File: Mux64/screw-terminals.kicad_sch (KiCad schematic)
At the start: 111 parts

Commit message: Add files via upload
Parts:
- gave numbers to parts that had none: 111

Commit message: Add files via upload
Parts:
- J11, J12, J13, J14, J15, J16, J17, J18: footprint (none) -> TerminalBlock_Phoenix:TerminalBlock_Phoenix_MPT-0,5-12-2.54_1x12_P2.54mm_Horizontal
- R10, R100, R101, R102, R103, R104, R105, R106, R107, R108, R109, R11, R110, R12, R13, R14, R15, R16, R17, R18, R19, R20, R21, R22, R23, R24, R25, R26, R27, R28, R29, R30, R31, R32, R39, R40, R41, R42, R43, R44, R45, R46, R47, R48, R49, R50, R57, R58, R59, R60, R61, R62, R63, R64, R65, R66, R67, R68, R69, R70, R71, R72, R73, R74, R75, R76, R77, R78, R79, R80, R81, R82, R83, R84, R85, R86, R87, R88, R89, R9, R90, R91, R92, R93, R94, R95, R96, R97, R98, R99: footprint (none) -> Resistor_SMD:R_0805_2012Metric
- R33, R34, R35, R36, R37, R38, R51, R52, R53, R54, R55, R56: footprint (none) -> Resistor_SMD:R_1206_3216Metric
- R8: footprint (none) -> Resistor_SMD:R_0603_1608Metric

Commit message: Add files via upload
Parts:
- removed R8: 0ohm, Resistor_SMD:R_0603_1608Metric, symbol Device:R_Small_US
- R21, R22, R23, R24, R25, R26: footprint Resistor_SMD:R_0805_2012Metric -> Resistor_SMD:R_1206_3216Metric
- R51, R52, R53, R54, R55, R56: footprint Resistor_SMD:R_1206_3216Metric -> Resistor_SMD:R_0805_2012Metric
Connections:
- net MUX64_A14 is gone; now on net MUX64_A18: R66.2, R77.1
- net MUX64_A28 is gone; now on net MUX64_A29: R49.2, R61.1
- net MUX64_A34 is gone; now on net MUX64_A22: R44.2, R55.1
- net MUX64_A36 is gone; now on net MUX64_A41: R15.2, R27.1
- net MUX64_A10: now also R72.2, R84.1; no longer R109.1, R97.2
- net MUX64_A11: now also R71.2, R83.1; no longer R110.1, R98.2
- net MUX64_A12: now also R70.2, R82.1; no longer R63.2, R75.1
- net MUX64_A13: now also R64.2, R81.1; no longer R65.2, R76.1
- net MUX64_A15: now also R65.2, R76.1; no longer R67.2, R78.1
- net MUX64_A16: now also R63.2, R75.1; no longer R68.2, R79.1
- net MUX64_A17: now also R67.2, R78.1; no longer R69.2, R80.1
- net MUX64_A18: no longer R64.2, R81.1
- net MUX64_A19: now also R69.2, R80.1; no longer R70.2, R82.1
- net MUX64_A2: now also R110.1, R98.2; no longer R101.1, R90.2
- net MUX64_A20: now also R68.2, R79.1; no longer R71.2, R83.1
- net MUX64_A21: now also R45.2, R56.1; no longer R72.2, R84.1
- net MUX64_A22: no longer R73.2, R85.1
- net MUX64_A23: now also R43.2, R54.1; no longer R74.2, R86.1
- net MUX64_A24: now also R42.2, R53.1; no longer R40.2, R57.1
- net MUX64_A25: now also R41.2, R52.1; no longer R46.2, R58.1
- net MUX64_A26: now also R39.2, R51.1; no longer R47.2, R59.1
- net MUX64_A27: now also R50.2, R62.1; no longer R48.2, R60.1
- net MUX64_A29: no longer R50.2, R62.1
- net MUX64_A3: now also R109.1, R97.2; no longer R102.1, R91.2
- net MUX64_A30: now also R48.2, R60.1; no longer R39.2, R51.1
- net MUX64_A31: now also R47.2, R59.1; no longer R41.2, R52.1
- net MUX64_A32: now also R46.2, R58.1; no longer R42.2, R53.1
- net MUX64_A33: now also R40.2, R57.1; no longer R43.2, R54.1
- net MUX64_A35: now also R20.2, R32.1; no longer R45.2, R56.1
- net MUX64_A37: now also R19.2, R31.1; no longer R16.2, R28.1
- net MUX64_A38: now also R18.2, R30.1; no longer R17.2, R29.1
- net MUX64_A39: now also R17.2, R29.1; no longer R18.2, R30.1
- net MUX64_A4: now also R108.1, R96.2; no longer R103.1, R92.2
- net MUX64_A40: now also R16.2, R28.1; no longer R19.2, R31.1
- net MUX64_A41: no longer R20.2, R32.1
- net MUX64_A43: now also R14.2, R26.1; no longer R21.1, R9.2
- net MUX64_A45: now also R13.2, R25.1; no longer R10.2, R22.1
- net MUX64_A47: now also R12.2, R24.1; no longer R11.2, R23.1
- net MUX64_A49: now also R11.2, R23.1; no longer R12.2, R24.1
- net MUX64_A5: now also R107.1, R95.2; no longer R104.1, R93.2
- net MUX64_A51: now also R10.2, R22.1; no longer R13.2, R25.1
- net MUX64_A53: now also R21.1, R9.2; no longer R14.2, R26.1
- net MUX64_A6: now also R106.1, R94.2; no longer R105.1, R88.2
- net MUX64_A7: now also R105.1, R88.2; no longer R106.1, R94.2
- net MUX64_A8: now also R74.2, R86.1; no longer R107.1, R95.2
- net MUX64_A9: now also R73.2, R85.1; no longer R108.1, R96.2
- net MUX64_A0 renamed MUX64_A60
- net MUX64_A1 renamed MUX64_A57
- new net MUX64_A54: R104.1, R93.2
- new net MUX64_A55: R102.1, R91.2
- new net MUX64_A56: R103.1, R92.2
- new net MUX64_A58: R101.1, R90.2
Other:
- note removed: "Unused Mux inputs"

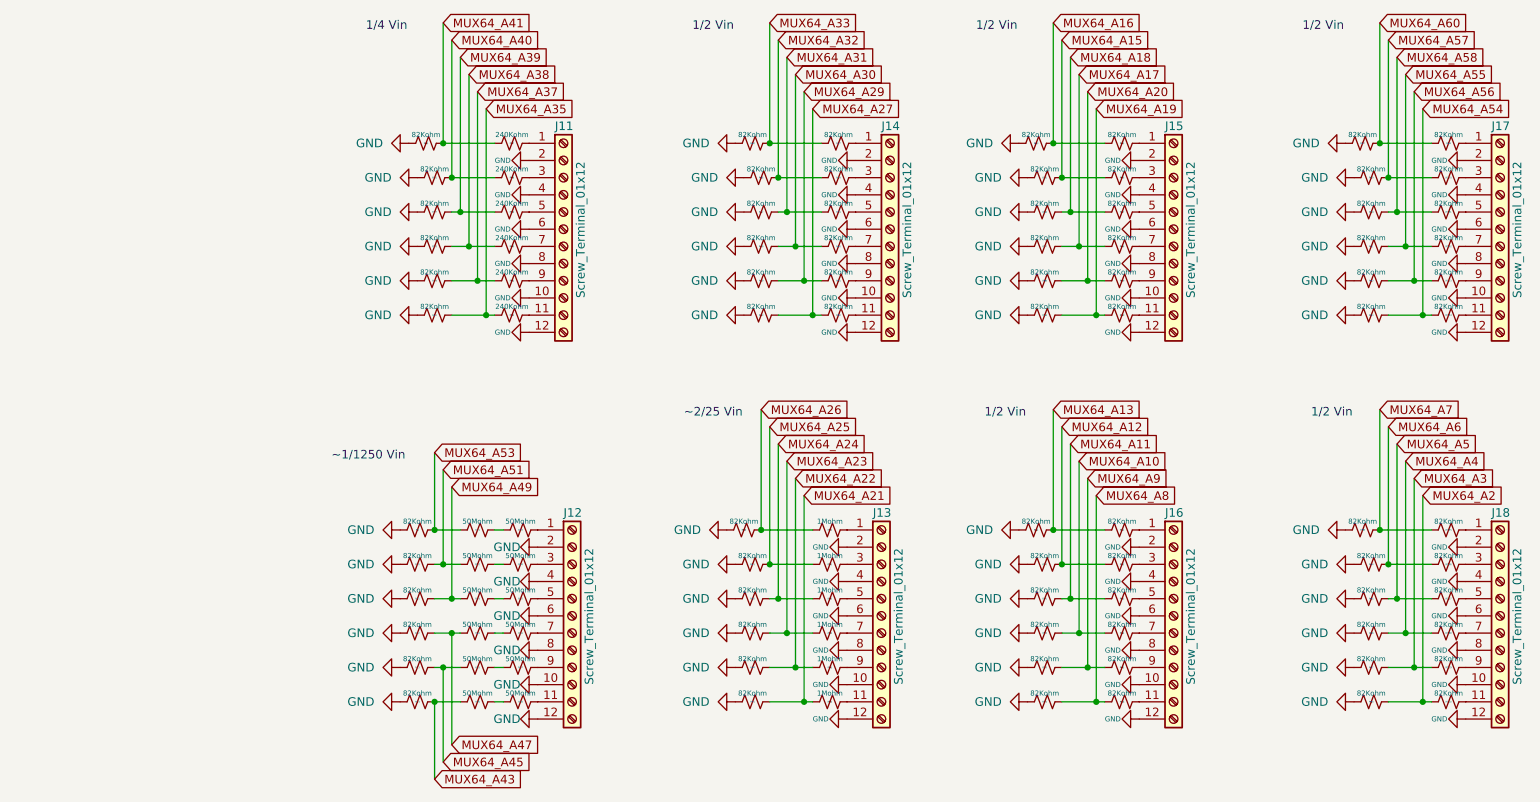
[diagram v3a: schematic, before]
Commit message: Final revision
Fixed high voltage spacial issue and distributed traces to have less density on the bottom of the board
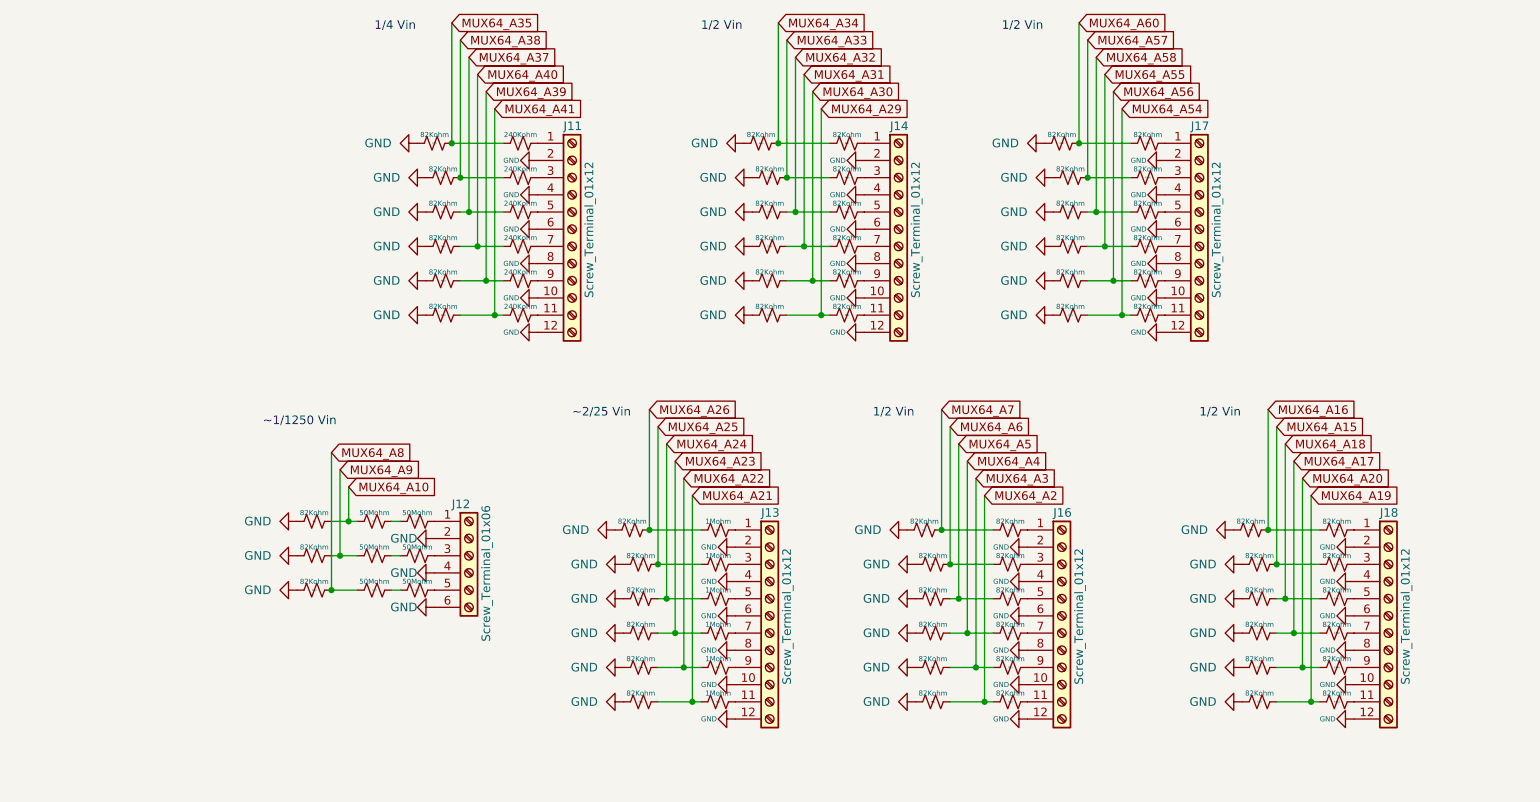
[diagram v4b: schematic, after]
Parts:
- removed J12, J15: Screw_Terminal_01x12, TerminalBlock_Phoenix:TerminalBlock_Phoenix_MPT-0,5-12-2.54_1x12_P2.54mm_Horizontal, symbol Connector:Screw_Terminal_01x12
- removed R23, R24, R25, R26, R33, R34, R35, R36, R37, R38: 50Mohm, Resistor_SMD:R_1206_3216Metric, symbol Device:R_Small_US
- removed R63, R65, R66, R67, R68, R69, R75, R76, R77, R78, R79, R80: 82Kohm, Resistor_SMD:R_0805_2012Metric, symbol Device:R_Small_US
- added J12: Screw_Terminal_01x06, TerminalBlock_RND:TerminalBlock_RND_205-00071_1x06_P7.50mm_Horizontal, symbol Connector:Screw_Terminal_01x06
- added R8: 82Kohm, Resistor_SMD:R_0805_2012Metric, symbol Device:R_Small_US
- R11, R12, R13, R14: value 82Kohm -> 50Mohm; footprint Resistor_SMD:R_0805_2012Metric -> Resistor_SMD:R_1206_3216Metric
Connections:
- net MUX64_A11 is gone; now on net MUX64_A5: R71.2, R83.1
- net MUX64_A12 is gone; now on net MUX64_A6: R70.2, R82.1
- net MUX64_A13 is gone; now on net MUX64_A7: R64.2, R81.1
- net MUX64_A27 is gone; now on net MUX64_A29: R50.2, R62.1
- net GND: now also J12.2 (Pin_2), J12.4 (Pin_4), J12.6 (Pin_6), R8.1; no longer R11.1, R12.1, R13.1, R14.1
- net MUX64_A10: now also R11.1, R8.2; no longer R72.2, R84.1
- net MUX64_A15: now also R106.1, R94.2
- net MUX64_A16: now also R105.1, R88.2
- net MUX64_A17: now also R108.1, R96.2
- net MUX64_A18: now also R107.1, R95.2
- net MUX64_A19: now also R110.1, R98.2
- net MUX64_A2: now also R74.2, R86.1; no longer R110.1, R98.2
- net MUX64_A20: now also R109.1, R97.2
- net MUX64_A29: no longer R49.2, R61.1
- net MUX64_A3: now also R73.2, R85.1; no longer R109.1, R97.2
- net MUX64_A30: now also R49.2, R61.1; no longer R48.2, R60.1
- net MUX64_A31: now also R48.2, R60.1; no longer R47.2, R59.1
- net MUX64_A32: now also R47.2, R59.1; no longer R46.2, R58.1
- net MUX64_A33: now also R46.2, R58.1; no longer R40.2, R57.1
- net MUX64_A35: now also R15.2, R27.1; no longer R20.2, R32.1
- net MUX64_A37: now also R17.2, R29.1; no longer R19.2, R31.1
- net MUX64_A38: now also R16.2, R28.1; no longer R18.2, R30.1
- net MUX64_A39: now also R19.2, R31.1; no longer R17.2, R29.1
- net MUX64_A4: now also R72.2, R84.1; no longer R108.1, R96.2
- net MUX64_A40: now also R18.2, R30.1; no longer R16.2, R28.1
- net MUX64_A41: now also R20.2, R32.1; no longer R15.2, R27.1
- net MUX64_A5: no longer R107.1, R95.2
- net MUX64_A6: no longer R106.1, R94.2
- net MUX64_A7: no longer R105.1, R88.2
- net MUX64_A8: now also R10.2, R13.1; no longer R74.2, R86.1
- net MUX64_A9: now also R12.1, R9.2; no longer R73.2, R85.1
- net at R21.2: now also J12.3 (Pin_3)
- net at R22.2: now also J12.5 (Pin_5)
- net MUX64_A43: no longer names the net of R14.2
- net MUX64_A43: now also J12.1 (Pin_1)
- net MUX64_A45: no longer names the net of R13.2
- net MUX64_A45: now also R22.1
- net MUX64_A47: no longer names the net of R12.2
- net MUX64_A47: now also R21.1
- net MUX64_A49: no longer names the net of R11.2
- net MUX64_A49: now also R14.1
- removed net MUX64_A51: R10.2, R22.1
- removed net MUX64_A53: R21.1, R9.2
- new net MUX64_A34: R40.2, R57.1
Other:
- moved on the sheet: J11, J13, J14, J16, J17, J18, R100, R101, R102, R103, R104, R105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

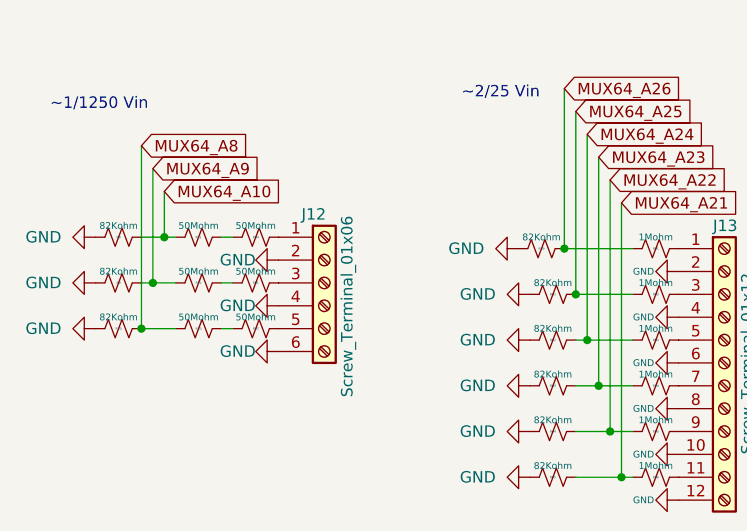
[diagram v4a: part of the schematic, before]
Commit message: Power and Ground traces resized
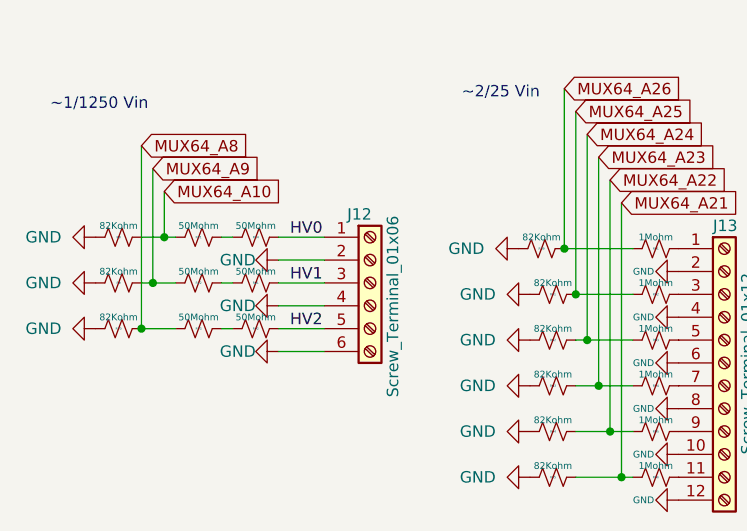
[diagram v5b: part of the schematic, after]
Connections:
- net HV2: now reaches J12.5 (Pin_5), R22.2
- net HV1: now reaches J12.3 (Pin_3), R21.2
- net HV0: now reaches J12.1 (Pin_1), R14.2
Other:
- moved on the sheet: J12
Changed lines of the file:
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@@
+    (stroke (width 0) (type default) (color 0 0 0 0))
+  )
+  (wire (pts (xy 90.17 118.11) (xy 85.09 118.11))
     (stroke (width 0) (type default) (color 0 0 0 0))
   )
@@
     (stroke (width 0) (type default) (color 0 0 0 0))
   )
+  (wire (pts (xy 90.17 113.03) (xy 85.09 113.03))
+    (stroke (width 0) (type default) (color 0 0 0 0))
+  )
   (wire (pts (xy 162.56 96.52) (xy 162.56 119.38))
     (stroke (width 0) (type default) (color 0 0 0 0))
@@
     (stroke (width 0) (type default) (color 0 0 0 0))
   )
+  (wire (pts (xy 90.17 107.95) (xy 85.09 107.95))
+    (stroke (width 0) (type default) (color 0 0 0 0))
+  )
   (wire (pts (xy 90.17 39.37) (xy 90.17 62.23))
     (stroke (width 0) (type default) (color 0 0 0 0))
@@
     (stroke (width 0) (type default) (color 0 0 0 0))
   )
+  (wire (pts (xy 90.17 120.65) (xy 85.09 120.65))
+    (stroke (width 0) (type default) (color 0 0 0 0))
+  )
   (wire (pts (xy 135.89 52.07) (xy 135.89 34.29))
     (stroke (width 0) (type default) (color 0 0 0 0))
@@
     (stroke (width 0) (type default) (color 0 0 0 0))
   )
+  (wire (pts (xy 90.17 115.57) (xy 85.09 115.57))
+    (stroke (width 0) (type default) (color 0 0 0 0))
+  )
   (wire (pts (xy 72.39 107.95) (xy 72.39 102.87))
     (stroke (width 0) (type default) (color 0 0 0 0))
@@
   )
   (wire (pts (xy 78.74 107.95) (xy 80.01 107.95))
+    (stroke (width 0) (type default) (color 0 0 0 0))
+  )
+  (wire (pts (xy 90.17 110.49) (xy 85.09 110.49))
     (stroke (width 0) (type default) (color 0 0 0 0))
   )
@@
   )
   (text "1/2 Vin" (at 198.12 92.71 0)
+    (effects (font (size 1.27 1.27)) (justify left bottom))
+  )
+  (label "HV0" (at 86.36 107.95 0)
+    (effects (font (size 1.27 1.27)) (justify left bottom))
+  )
+  (label "HV1" (at 86.36 113.03 0)
+    (effects (font (size 1.27 1.27)) (justify left bottom))
+  )
+  (label "HV2" (at 86.36 118.11 0)
     (effects (font (size 1.27 1.27)) (justify left bottom))
   )
@@
     (pin "1")
   )
-  (symbol (lib_id "Connector:Screw_Terminal_01x06") (at 90.17 113.03 0) (unit 1)
-    (in_bom yes) (on_board yes)
-    (property "Reference" "J12" (id 0) (at 87.63 105.41 0)
+  (symbol (lib_id "Connector:Screw_Terminal_01x06") (at 95.25 113.03 0) (unit 1)
+    (in_bom yes) (on_board yes)
+    (property "Reference" "J12" (id 0) (at 92.71 105.41 0)
       (effects (font (size 1.27 1.27)) (justify left))
     )
-    (property "Value" "Screw_Terminal_01x06" (id 1) (at 92.71 125.73 90)
+    (property "Value" "Screw_Terminal_01x06" (id 1) (at 97.79 125.73 90)
       (effects (font (size 1.27 1.27)) (justify left))
     )
-    (property "Footprint" "TerminalBlock_RND:TerminalBlock_RND_205-00071_1x06_P7.50mm_Horizontal" (id 2) (at 90.17 113.03 0)
-      (effects (font (size 1.27 1.27)) hide)
-    )
-    (property "Datasheet" "~" (id 3) (at 90.17 113.03 0)
-      (effects (font (size 1.27 1.27)) hide)
-    )
+    (property "Footprint" "TerminalBlock_RND:TerminalBlock_RND_205-00071_1x06_P7.50mm_Horizontal" (id 2) (at 95.25 113.03 0)
+      (effects (font (size 1.27 1.27)) hide)
+    )
+    (property "Datasheet" "~" (id 3) (at 95.25 113.03 0)
+      (effects (font (size 1.27 1.27)) hide)
+    )
